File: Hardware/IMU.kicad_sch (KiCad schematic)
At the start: 4 parts

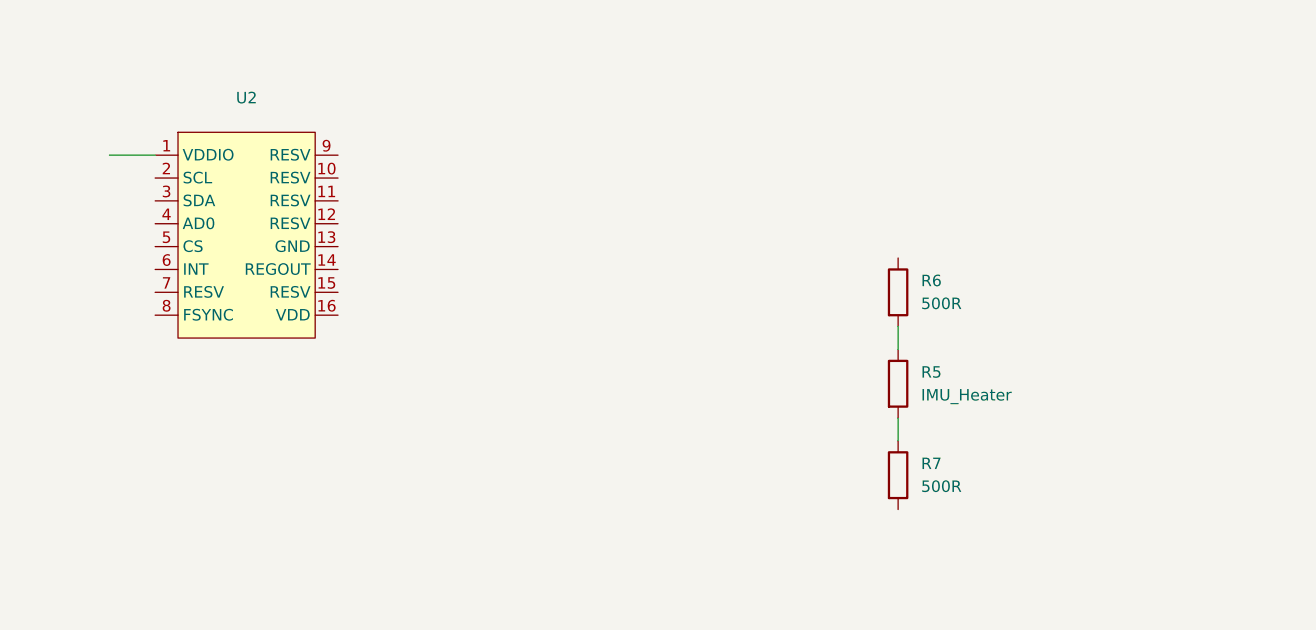
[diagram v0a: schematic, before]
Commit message: Finished IMU SCH
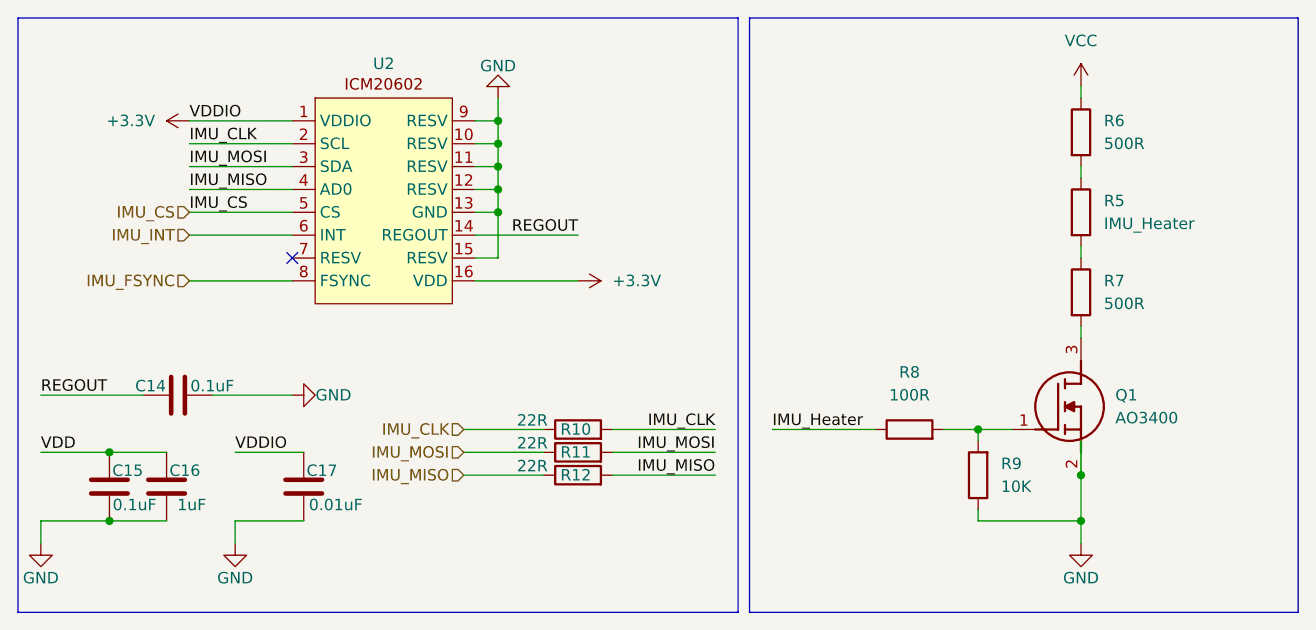
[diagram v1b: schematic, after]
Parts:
- added C14, C15: 0.1uF, symbol Device:C
- added C16: 1uF, symbol Device:C
- added C17: 0.01uF, symbol Device:C
- added Q1: AO3400, SOT95P280X125-3N, symbol SamacSys_Parts:AO3400
- added R10, R11, R12: 22R, symbol Device:R
- added R8: 100R, symbol Device:R
- added R9: 10K, symbol Device:R
- U2: footprint (none) -> SamacSys_Parts:ICM20602
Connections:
- net at R7.2: now also Q1.3 (D)
- net VCC: now reaches R6.1
- net +3.3V: now reaches U2.1 (VDDIO)
- net +3.3V: now also U2.16 (VDD), C17.2
- net GND: now reaches U2.10 (RESV)
- net GND: now also U2.11 (RESV), U2.12 (RESV), U2.13 (GND), U2.15 (RESV), U2.9 (RESV), C14.2, C15.1, C16.1, C17.1, Q1.2 (S), R9.1
- net REGOUT: now reaches U2.14 (REGOUT)
- net REGOUT: now also C14.1
- net IMU_CLK: now reaches U2.2 (SCL)
- net IMU_CLK: now also R10.1, R10.2
- net IMU_MOSI: now reaches U2.3 (SDA)
- net IMU_MOSI: now also R11.1, R11.2
- net IMU_MISO: now reaches U2.4 (AD0)
- net IMU_MISO: now also R12.1, R12.2
- net IMU_CS: now reaches U2.5 (CS)
- net IMU_INT: now reaches U2.6 (INT)
- net IMU_FSYNC: now reaches U2.8 (FSYNC)
- new net: Q1.1 (G), R8.2, R9.2
- new net IMU_Heater: R8.1
- new net VDD: C15.2, C16.2
- no-connect marks 0 -> 1
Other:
- moved on the sheet: R5, R6, R7
